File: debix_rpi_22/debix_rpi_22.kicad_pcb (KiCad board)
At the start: 2 copper layers, 2 parts, among them J1 Conn_01x24, J3 RPi 22 Pin MIPI CSI-2

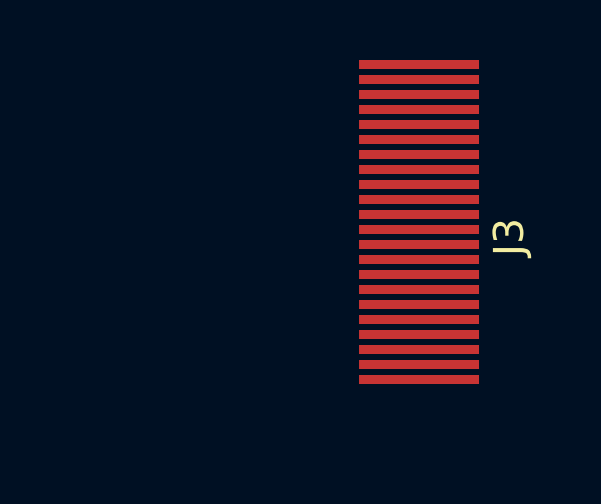
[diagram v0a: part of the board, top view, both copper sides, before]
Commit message: corrected positions of right side of cable.
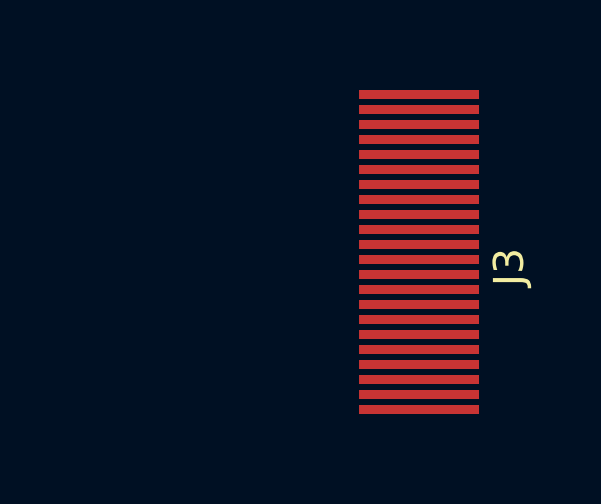
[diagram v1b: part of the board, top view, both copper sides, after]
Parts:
- moved J3 1.00 mm to (178.0, 135.8)
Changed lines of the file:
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@@
 	(footprint "VoXel:fpc_1x22-P0.5mm_pins_only"
 		(layer "F.Cu")
-		(at 178 134.75 -90)
+		(at 178 135.75 -90)
 		(descr "24 pin FPC connector")
 		(property "Reference" "J3"

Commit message: just the lanes.
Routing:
- net /csi_d3_P: track 0.00 -> 67.9 mm
- net /csi_d3_N: track 0.00 -> 67.9 mm
- net /csi_d2_P: track 0.00 -> 67.9 mm
- net /csi_d2_N: track 0.00 -> 67.9 mm
- net /csi_d1_P: track 0.00 -> 67.9 mm
- net /csi_d1_N: track 0.00 -> 67.9 mm
- net /csi_d0_P: track 0.00 -> 67.9 mm
- net /csi_d0_N: track 0.00 -> 67.9 mm
- net /csi_clk_P: track 0.00 -> 67.9 mm
- net /csi_clk_N: track 0.00 -> 67.9 mm
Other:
- board outline added: 71 x 12.5 mm

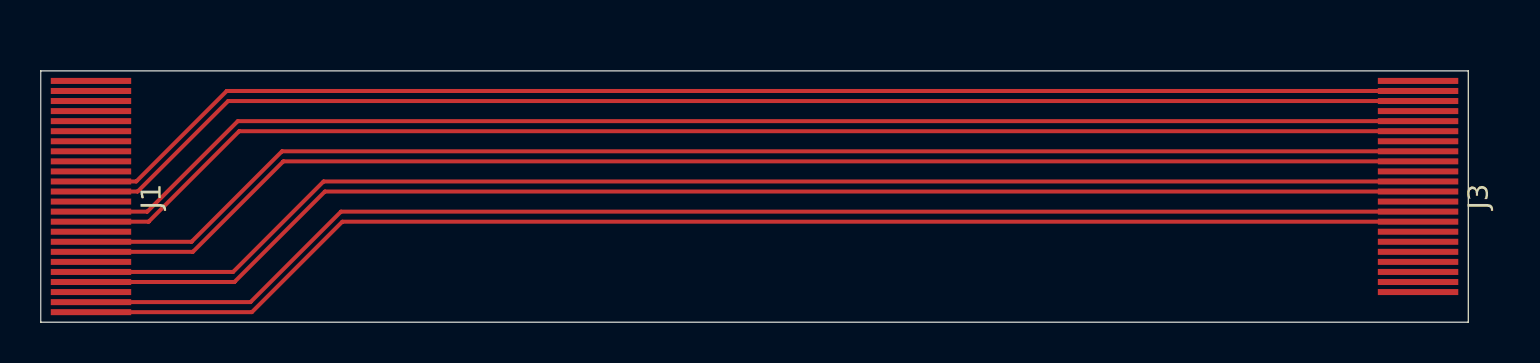
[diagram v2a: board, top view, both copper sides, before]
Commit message: hand routing finished.
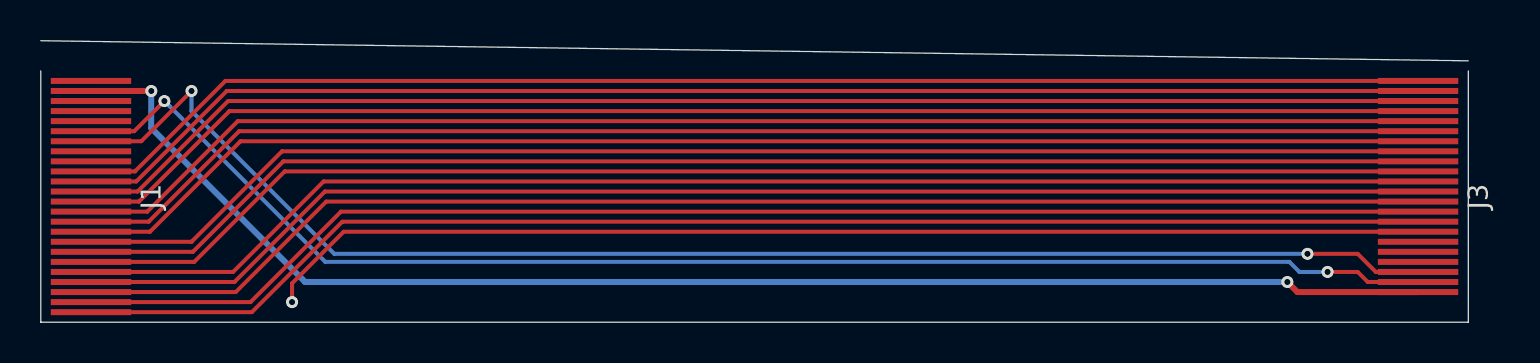
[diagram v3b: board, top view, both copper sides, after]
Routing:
- net GND: track 0.00 -> 397.4 mm, vias 0 -> 1
- net /csi_scl: track 0.00 -> 71.3 mm, vias 0 -> 2
- net +3V3: track 0.00 -> 71.2 mm, vias 0 -> 2
- net /csi_sda: track 0.00 -> 70.4 mm, vias 0 -> 2
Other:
- board size 71 x 12.5 mm -> 71 x 14 mm

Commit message: teardrops new ground plane connected via
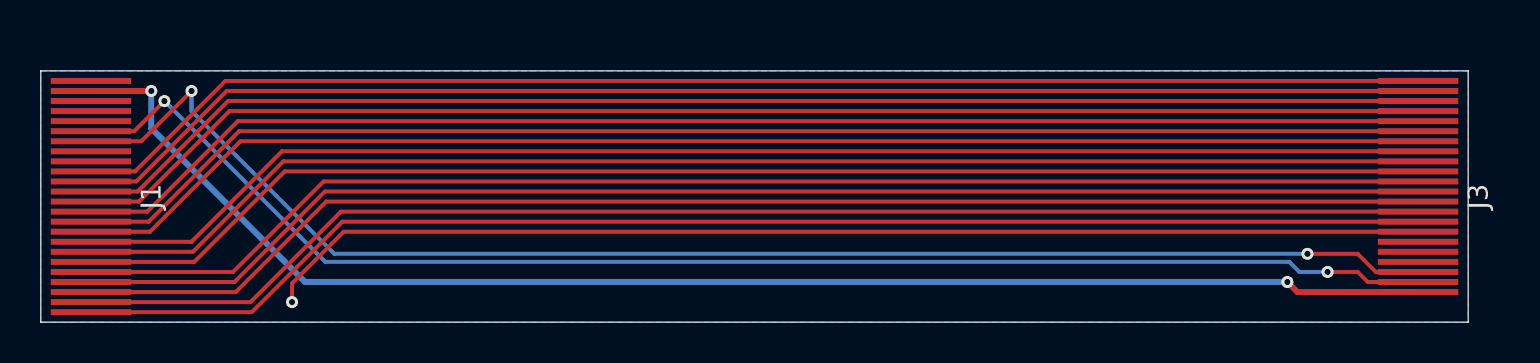
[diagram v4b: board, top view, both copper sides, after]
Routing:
- added copper zone on B.Cu, net GND
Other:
- board size 71 x 14 mm -> 71 x 12.5 mm

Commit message: rerouted with the two new gpio pins connected. A bit of a mess. But should work.
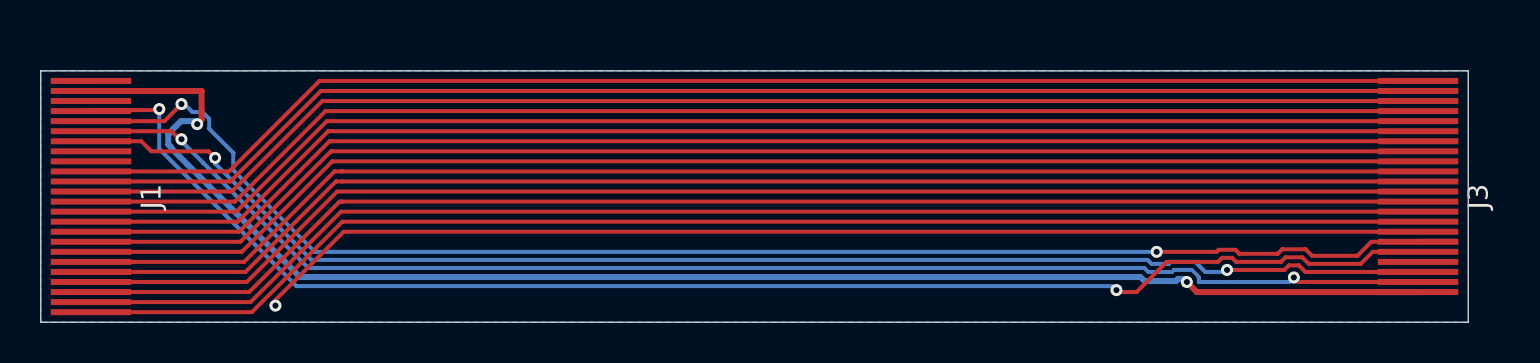
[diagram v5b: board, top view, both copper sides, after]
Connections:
- J1 pad 4: unconnected-(J1-Pin_4-Pad4) -> /CAM_GPIO_1
- J1 pad 5: unconnected-(J1-Pin_5-Pad5) -> /CAM_GPIO_0
- J3 pad 17: unconnected-(J3-Pin_17-Pad17) -> /CAM_GPIO_0
- J3 pad 18: unconnected-(J3-Pin_18-Pad18) -> /CAM_GPIO_1
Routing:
- net /CAM_GPIO_0: track 0.00 -> 72.8 mm, vias 0 -> 2
- net /CAM_GPIO_1: track 0.00 -> 72.3 mm, vias 0 -> 2
- net +3V3: track 71.2 -> 74.8 mm
- net /csi_scl: track 71.3 -> 69.2 mm
- net /csi_sda: track 70.4 -> 69.7 mm
